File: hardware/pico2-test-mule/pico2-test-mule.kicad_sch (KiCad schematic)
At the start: 70 parts, among them J2 SPEAKER, J4 POWER, J5 EXT_CAP, J6 RAILS, J7 AUX, J8 MOTOR, Q1 DMN2991UDA-7B, Q10 SS8050, Q11 SS8050, Q12 SS8050, Q13 SS8050, Q2 DMN2991UDA-7B, Q3 NST847BPDP6T5G, Q4 NST847BPDP6T5G, Q5 DMN2991UDA-7B, Q6 DMN2991UDA-7B, Q7 DMN2991UDA-7B, Q8 DMN2991UDA-7B, Q9 SS8050, U1 NCS2220AMUT1G, U2 AP63203WU, U5 MAX98357AEWL+T, U6 MD9927, U7 PICO

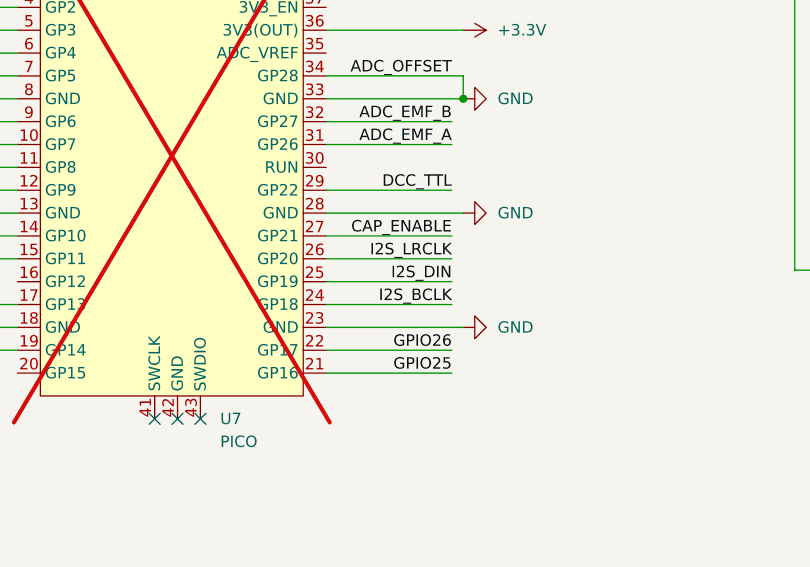
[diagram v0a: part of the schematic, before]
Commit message: chore: reorder i2s gpios
chore: add qr code to silkscreen
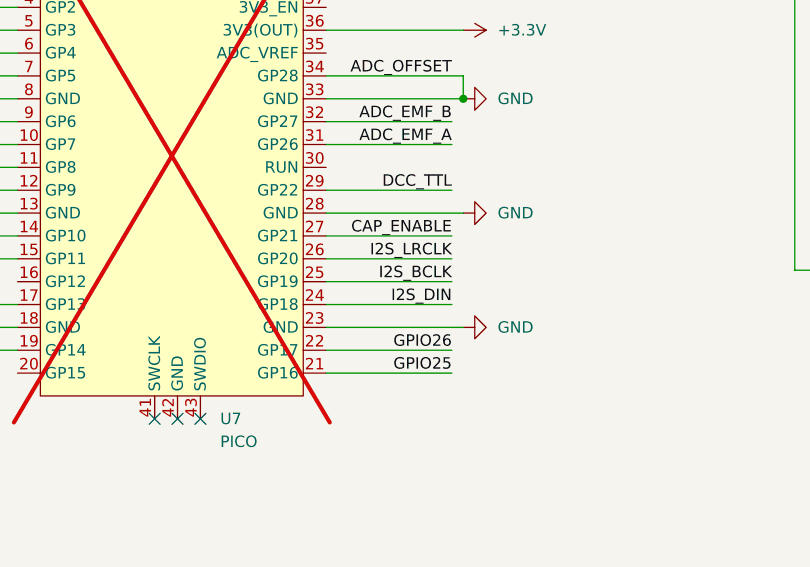
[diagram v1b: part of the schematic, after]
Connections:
- net I2S_BCLK: now also U7.25 (GP19); no longer U7.24 (GP18)
- net I2S_DIN: now also U7.24 (GP18); no longer U7.25 (GP19)
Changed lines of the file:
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@@
 	)
 	(label "I2S_DIN"
-		(at 285.75 173.99 180)
+		(at 285.75 176.53 180)
 		(effects
 			(font
@@
 	)
 	(label "I2S_BCLK"
-		(at 285.75 176.53 180)
+		(at 285.75 173.99 180)
 		(effects
 			(font
